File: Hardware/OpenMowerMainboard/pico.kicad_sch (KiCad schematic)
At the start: 6 parts, among them U10 74HC4051, U11 Pico, U7 SN74LV1T34DBV, U9 74HC4051

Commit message: BoM data added to kicad - results exported to .xlsx file
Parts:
- C25: Digikey (none) -> 490-4789-1-ND; Part Number (none) -> GCM21BR72A104KA37L; Stock_PN (none) -> C-805-.1uF-100V-X7R
- D25: Digikey (none) -> 1568-COM-16347CT-ND; Part Number (none) -> COM-16347; Stock_PN (none) -> LED-WS2812B
- U10, U9: Digikey (none) -> 1727-3064-1-ND; Part Number (none) -> 74HC4051PW,118; Stock_PN (none) -> U-74HC4051
- U11: Digikey (none) -> 2648-SC0915CT-ND; Part Number (none) -> SC0915; Stock_PN (none) -> U-RP2040-PCB
- U7: Digikey (none) -> 296-SN74LV1T34DBVRG4CT-ND; Part Number (none) -> SN74LV1T34DBVRG4; Stock_PN (none) -> U-SN74LV1T34
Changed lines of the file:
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@@
+      (effects (font (size 1.27 1.27)) hide)
+    )
+    (property "Digikey" "1727-3064-1-ND" (id 4) (at 48.895 93.98 0)
+      (effects (font (size 1.27 1.27)) hide)
+    )
+    (property "Part Number" "74HC4051PW,118" (id 5) (at 48.895 93.98 0)
+      (effects (font (size 1.27 1.27)) hide)
+    )
+    (property "Stock_PN" "U-74HC4051" (id 6) (at 48.895 93.98 0)
       (effects (font (size 1.27 1.27)) hide)
     )
@@
       (effects (font (size 1.27 1.27)) hide)
     )
+    (property "Digikey" "296-SN74LV1T34DBVRG4CT-ND" (id 4) (at 132.715 159.385 0)
+      (effects (font (size 1.27 1.27)) hide)
+    )
+    (property "Part Number" "SN74LV1T34DBVRG4" (id 5) (at 132.715 159.385 0)
+      (effects (font (size 1.27 1.27)) hide)
+    )
+    (property "Stock_PN" "U-SN74LV1T34" (id 6) (at 132.715 159.385 0)
+      (effects (font (size 1.27 1.27)) hide)
+    )
     (pin "1")
     (pin "2")
@@
     )
     (property "Datasheet" "~" (id 3) (at 160.655 165.1 0)
+      (effects (font (size 1.27 1.27)) hide)
+    )
+    (property "Digikey" "490-4789-1-ND" (id 4) (at 160.655 165.1 0)
+      (effects (font (size 1.27 1.27)) hide)
+    )
+    (property "Part Number" "GCM21BR72A104KA37L" (id 5) (at 160.655 165.1 0)
+      (effects (font (size 1.27 1.27)) hide)
+    )
+    (property "Stock_PN" "C-805-.1uF-100V-X7R" (id 6) (at 160.655 165.1 0)
       (effects (font (size 1.27 1.27)) hide)
     )
@@
       (effects (font (size 1.27 1.27)) (justify left top) hide)
     )
+    (property "Digikey" "1568-COM-16347CT-ND" (id 4) (at 173.99 159.385 0)
+      (effects (font (size 1.27 1.27)) hide)
+    )
+    (property "Part Number" "COM-16347" (id 5) (at 173.99 159.385 0)
+      (effects (font (size 1.27 1.27)) hide)
+    )
+    (property "Stock_PN" "LED-WS2812B" (id 6) (at 173.99 159.385 0)
+      (effects (font (size 1.27 1.27)) hide)
+    )
     (pin "1")
     (pin "2")
@@
     )
     (property "Datasheet" "http://www.ti.com/lit/ds/symlink/cd74hc4051.pdf" (id 3) (at 113.665 104.14 0)
+      (effects (font (size 1.27 1.27)) hide)
+    )
+    (property "Digikey" "1727-3064-1-ND" (id 4) (at 113.665 93.98 0)
+      (effects (font (size 1.27 1.27)) hide)
+    )
+    (property "Part Number" "74HC4051PW,118" (id 5) (at 113.665 93.98 0)
+      (effects (font (size 1.27 1.27)) hide)
+    )
+    (property "Stock_PN" "U-74HC4051" (id 6) (at 113.665 93.98 0)
       (effects (font (size 1.27 1.27)) hide)
     )
@@
       (effects (font (size 1.27 1.27)) hide)
     )
+    (property "Digikey" "2648-SC0915CT-ND" (id 4) (at 215.9 92.71 0)
+      (effects (font (size 1.27 1.27)) hide)
+    )
+    (property "Part Number" "SC0915" (id 5) (at 215.9 92.71 0)
+      (effects (font (size 1.27 1.27)) hide)
+    )
+    (property "Stock_PN" "U-RP2040-PCB" (id 6) (at 215.9 92.71 0)
+      (effects (font (size 1.27 1.27)) hide)
+    )

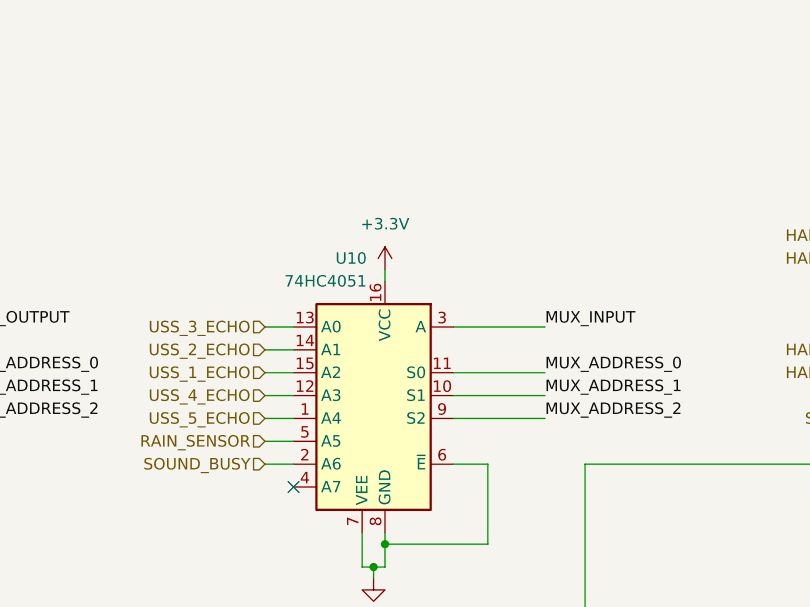
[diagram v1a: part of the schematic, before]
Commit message: added jumper for assembly without sound and ultrasonic sensors
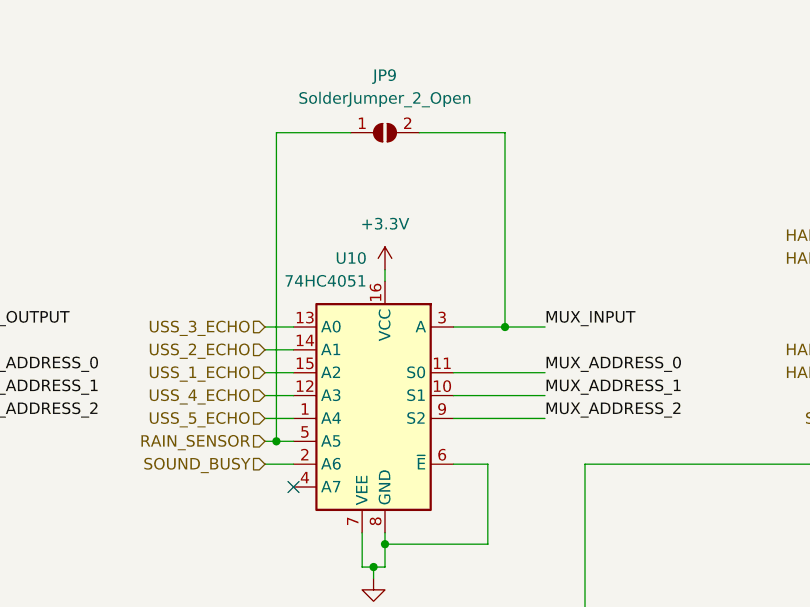
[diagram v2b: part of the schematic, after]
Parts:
- added JP9: SolderJumper_2_Open, Jumper:SolderJumper-2_P1.3mm_Open_RoundedPad1.0x1.5mm, symbol Jumper:SolderJumper_2_Open
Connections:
- net MUX_INPUT: now also JP9.2 (B)
- net RAIN_SENSOR: now also JP9.1 (A)
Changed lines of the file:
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@@
   (junction (at 160.655 170.815) (diameter 0) (color 0 0 0 0)
   )
+  (junction (at 101.6 99.06) (diameter 0) (color 0 0 0 0)
+  )
   (junction (at 112.395 113.03) (diameter 0) (color 0 0 0 0)
+  )
+  (junction (at 127 86.36) (diameter 0) (color 0 0 0 0)
   )
   (junction (at 191.77 86.36) (diameter 0) (color 0 0 0 0)
@@
     (stroke (width 0) (type default) (color 0 0 0 0))
   )
+  (wire (pts (xy 127 86.36) (xy 131.445 86.36))
+    (stroke (width 0) (type default) (color 0 0 0 0))
+  )
   (wire (pts (xy 113.665 109.22) (xy 113.665 110.49))
     (stroke (width 0) (type default) (color 0 0 0 0))
@@
     (stroke (width 0) (type default) (color 0 0 0 0))
   )
+  (wire (pts (xy 101.6 99.06) (xy 100.33 99.06))
+    (stroke (width 0) (type default) (color 0 0 0 0))
+  )
   (wire (pts (xy 32.385 93.98) (xy 38.735 93.98))
     (stroke (width 0) (type default) (color 0 0 0 0))
@@
     (stroke (width 0) (type default) (color 0 0 0 0))
   )
+  (wire (pts (xy 127 64.77) (xy 127 86.36))
+    (stroke (width 0) (type default) (color 0 0 0 0))
+  )
   (wire (pts (xy 191.77 86.36) (xy 198.12 86.36))
     (stroke (width 0) (type default) (color 0 0 0 0))
@@
     (stroke (width 0) (type default) (color 0 0 0 0))
   )
+  (wire (pts (xy 109.855 64.77) (xy 101.6 64.77))
+    (stroke (width 0) (type default) (color 0 0 0 0))
+  )
   (wire (pts (xy 56.515 93.98) (xy 66.675 93.98))
     (stroke (width 0) (type default) (color 0 0 0 0))
@@
     (stroke (width 0) (type default) (color 0 0 0 0))
   )
+  (wire (pts (xy 117.475 64.77) (xy 127 64.77))
+    (stroke (width 0) (type default) (color 0 0 0 0))
+  )
   (wire (pts (xy 112.395 113.03) (xy 112.395 114.3))
     (stroke (width 0) (type default) (color 0 0 0 0))
@@
     (stroke (width 0) (type default) (color 0 0 0 0))
   )
+  (wire (pts (xy 101.6 64.77) (xy 101.6 99.06))
+    (stroke (width 0) (type default) (color 0 0 0 0))
+  )
   (wire (pts (xy 173.99 104.14) (xy 198.12 104.14))
     (stroke (width 0) (type default) (color 0 0 0 0))
@@
     (stroke (width 0) (type default) (color 0 0 0 0))
   )
-  (wire (pts (xy 103.505 99.06) (xy 100.33 99.06))
+  (wire (pts (xy 103.505 99.06) (xy 101.6 99.06))
     (stroke (width 0) (type default) (color 0 0 0 0))
   )
@@
     (stroke (width 0) (type default) (color 0 0 0 0))
   )
-  (wire (pts (xy 121.285 86.36) (xy 131.445 86.36))
+  (wire (pts (xy 121.285 86.36) (xy 127 86.36))
     (stroke (width 0) (type default) (color 0 0 0 0))
   )
@@
     (pin "4")
   )
+  (symbol (lib_id "Jumper:SolderJumper_2_Open") (at 113.665 64.77 0) (unit 1)
+    (in_bom yes) (on_board yes) (fields_autoplaced)
+    (property "Reference" "JP9" (id 0) (at 113.665 58.42 0))
+    (property "Value" "SolderJumper_2_Open" (id 1) (at 113.665 60.96 0))
+    (property "Footprint" "Jumper:SolderJumper-2_P1.3mm_Open_RoundedPad1.0x1.5mm" (id 2) (at 113.665 64.77 0)
+      (effects (font (size 1.27 1.27)) hide)
+    )
+    (property "Datasheet" "~" (id 3) (at 113.665 64.77 0)
+      (effects (font (size 1.27 1.27)) hide)
+    )
+    (pin "1")
+    (pin "2")
+  )
   (symbol (lib_id "power:+3.3V") (at 113.665 80.01 0) (unit 1)

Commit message: feat(bom): added compatible lcsc codes, updated discontinued ones
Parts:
- D25: LCSC (none) -> C114586
- U7: LCSC (none) -> C1848228
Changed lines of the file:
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@@
+      (effects (font (size 1.27 1.27)) hide)
+    )
+    (property "LCSC" "C1848228" (id 7) (at 132.715 159.385 0)
       (effects (font (size 1.27 1.27)) hide)
     )
@@
       (effects (font (size 1.27 1.27)) hide)
     )
+    (property "LCSC" "C114586" (id 7) (at 173.99 159.385 0)
+      (effects (font (size 1.27 1.27)) hide)
+    )

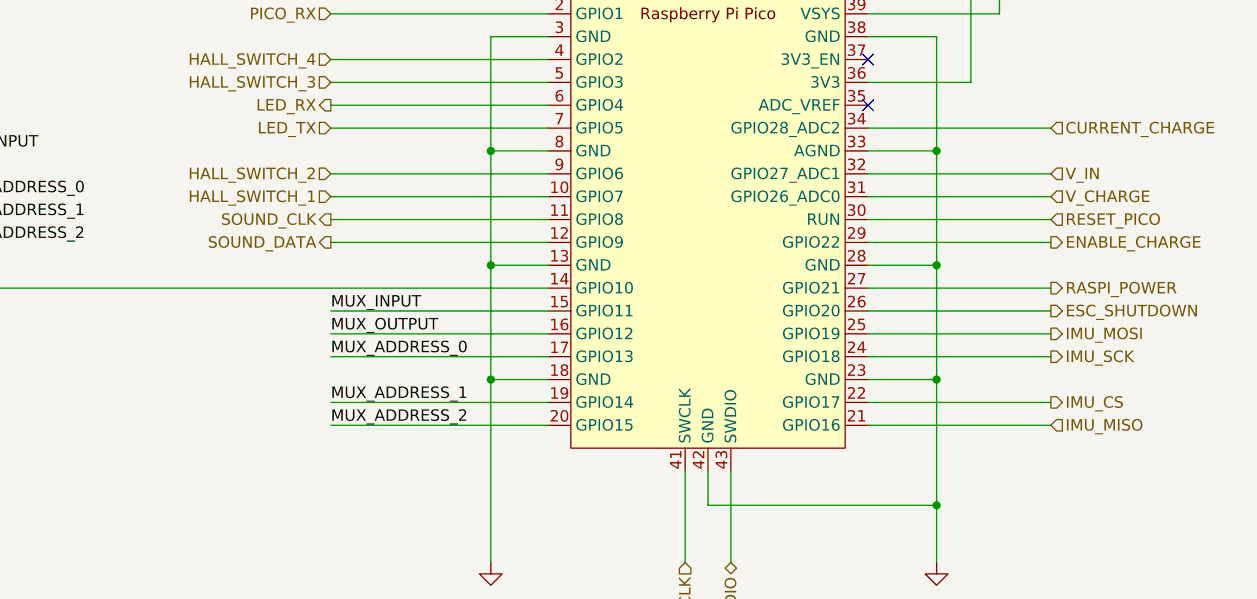
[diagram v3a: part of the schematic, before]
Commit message: feat(imu): switch GPIO pins 6-9 with 16-19
allows to use both MPU9250 and WT901 on the same header by routing UART pins to IMU header
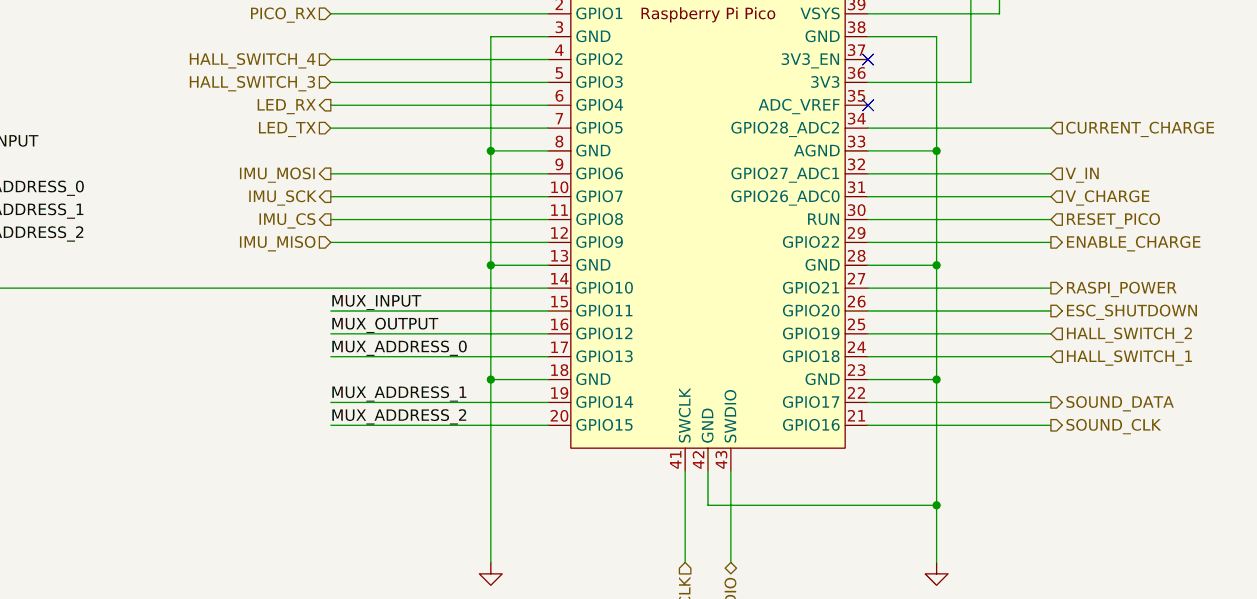
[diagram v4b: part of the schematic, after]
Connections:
- net HALL_SWITCH_1: now also U11.24 (GPIO18); no longer U11.10 (GPIO7)
- net HALL_SWITCH_2: now also U11.25 (GPIO19); no longer U11.9 (GPIO6)
- net IMU_CS: now also U11.11 (GPIO8); no longer U11.22 (GPIO17)
- net IMU_MISO: now also U11.12 (GPIO9); no longer U11.21 (GPIO16)
- net IMU_MOSI: now also U11.9 (GPIO6); no longer U11.25 (GPIO19)
- net IMU_SCK: now also U11.10 (GPIO7); no longer U11.24 (GPIO18)
- net SOUND_CLK: now also U11.21 (GPIO16); no longer U11.11 (GPIO8)
- net SOUND_DATA: now also U11.22 (GPIO17); no longer U11.12 (GPIO9)

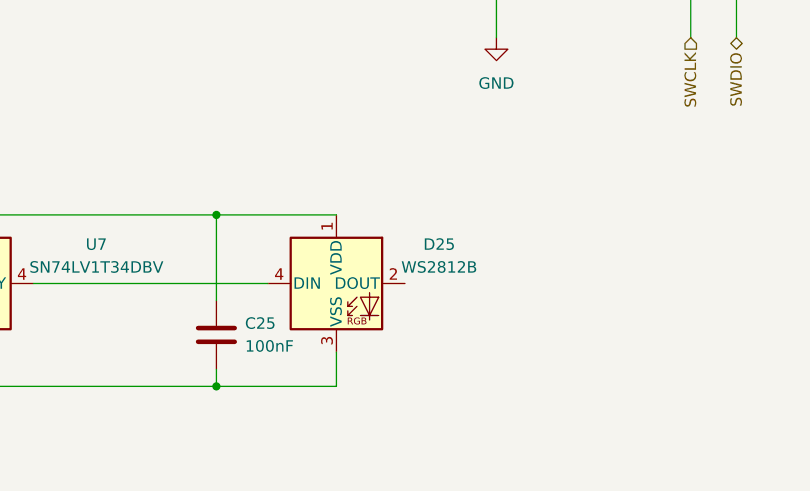
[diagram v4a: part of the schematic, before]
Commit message: fix: fixed ERC/DRC errors, removed LM2596S
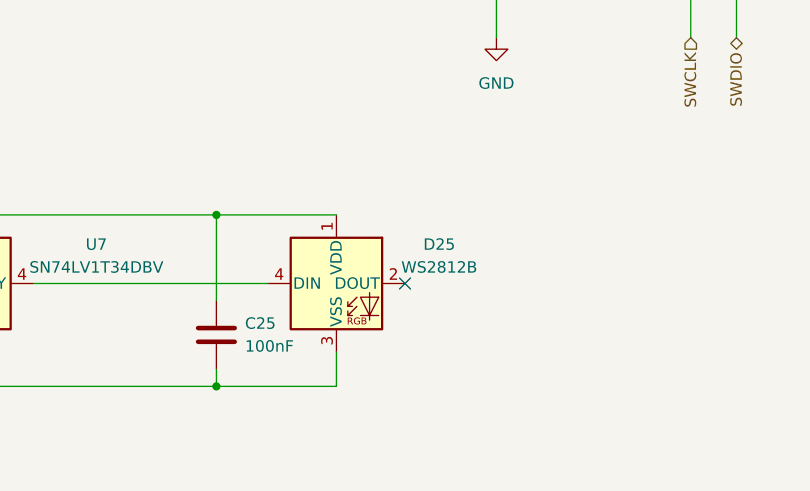
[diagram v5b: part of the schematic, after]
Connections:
- no-connect marks 7 -> 8
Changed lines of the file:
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@@
   (junction (at 132.715 170.815) (diameter 0) (color 0 0 0 0)
   )
+  (no_connect (at 181.61 159.385))
   (no_connect (at 38.735 99.06))
   (no_connect (at 38.735 104.14))

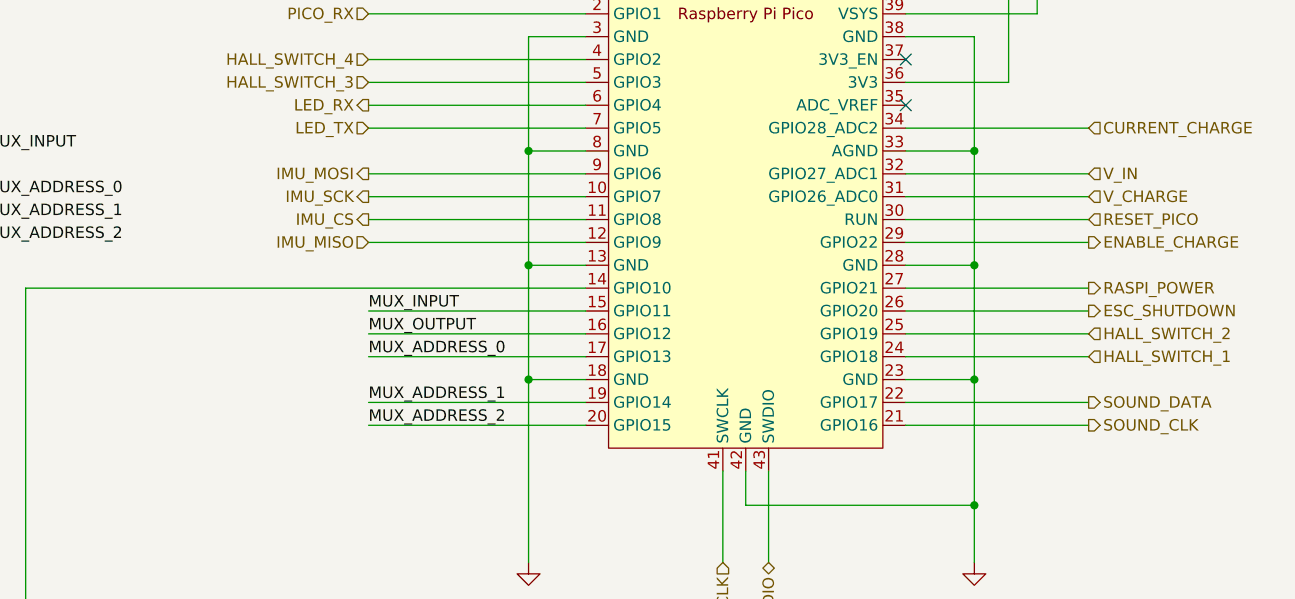
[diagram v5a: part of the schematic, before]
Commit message: fix(imu): update and reroute sound/imu connections
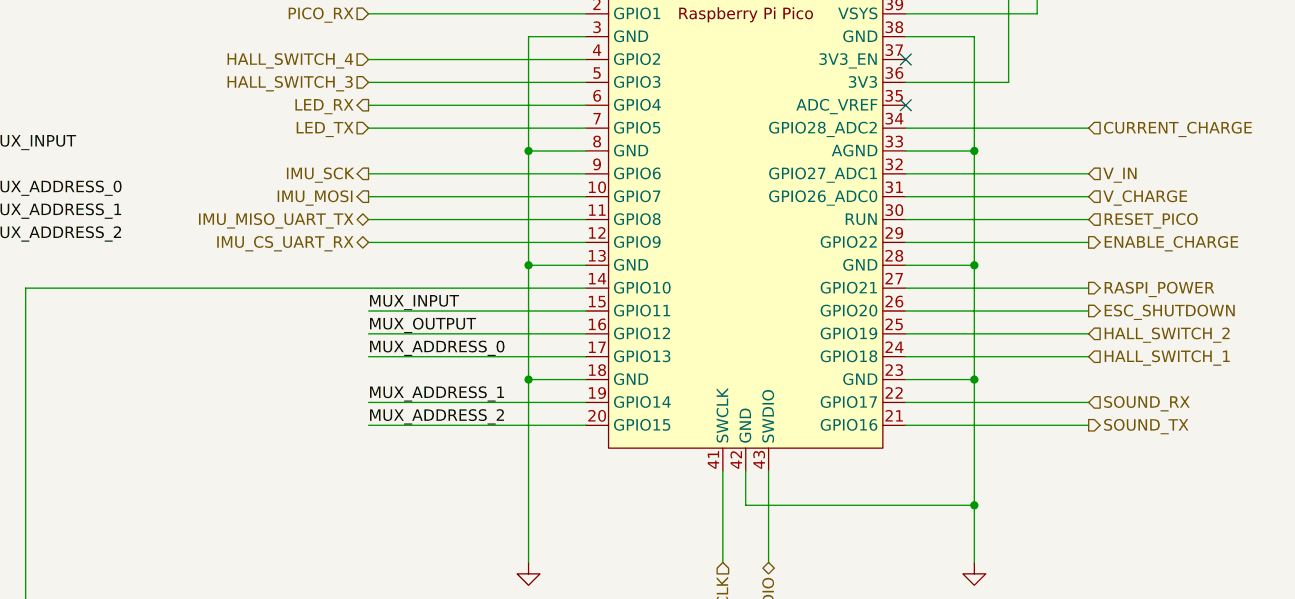
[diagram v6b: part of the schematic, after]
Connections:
- net IMU_MOSI: now also U11.10 (GPIO7); no longer U11.9 (GPIO6)
- net IMU_SCK: now also U11.9 (GPIO6); no longer U11.10 (GPIO7)
- net IMU_CS renamed IMU_MISO_UART_TX
- net IMU_MISO renamed IMU_CS_UART_RX
- net SOUND_CLK renamed SOUND_TX
- net SOUND_DATA renamed SOUND_RX
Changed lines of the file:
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@@
+    (effects (font (size 1.27 1.27)) (justify right))
+  )
+  (hierarchical_label "IMU_SCK" (shape output) (at 173.99 88.9 180)
     (effects (font (size 1.27 1.27)) (justify right))
   )
@@
   )
   (hierarchical_label "USS_3_TRIGGER" (shape output) (at 32.385 86.36 180)
-    (effects (font (size 1.27 1.27)) (justify right))
-  )
-  (hierarchical_label "IMU_MISO" (shape input) (at 173.99 96.52 180)
     (effects (font (size 1.27 1.27)) (justify right))
   )
@@
     (effects (font (size 1.27 1.27)) (justify right))
   )
-  (hierarchical_label "IMU_CS" (shape output) (at 173.99 93.98 180)
-    (effects (font (size 1.27 1.27)) (justify right))
-  )
   (hierarchical_label "RESET_PICO" (shape input) (at 254 93.98 0)
     (effects (font (size 1.27 1.27)) (justify left))
@@
     (effects (font (size 1.27 1.27)) (justify right))
   )
-  (hierarchical_label "SOUND_CLK" (shape output) (at 254 116.84 0)
+  (hierarchical_label "SOUND_TX" (shape output) (at 254 116.84 0)
     (effects (font (size 1.27 1.27)) (justify left))
   )
-  (hierarchical_label "IMU_SCK" (shape output) (at 173.99 91.44 180)
+  (hierarchical_label "IMU_MOSI" (shape output) (at 173.99 91.44 180)
     (effects (font (size 1.27 1.27)) (justify right))
   )
-  (hierarchical_label "IMU_MOSI" (shape output) (at 173.99 88.9 180)
+  (hierarchical_label "IMU_CS_UART_RX" (shape bidirectional) (at 173.99 96.52 180)
     (effects (font (size 1.27 1.27)) (justify right))
   )
@@
     (effects (font (size 1.27 1.27)) (justify left))
   )
-  (hierarchical_label "SOUND_DATA" (shape output) (at 254 114.3 0)
+  (hierarchical_label "SOUND_RX" (shape input) (at 254 114.3 0)
     (effects (font (size 1.27 1.27)) (justify left))
   )
@@
     (effects (font (size 1.27 1.27)) (justify left))
   )
+  (hierarchical_label "IMU_MISO_UART_TX" (shape bidirectional) (at 173.99 93.98 180)
+    (effects (font (size 1.27 1.27)) (justify right))
+  )
   (hierarchical_label "HALL_SWITCH_3" (shape input) (at 173.99 78.74 180)
